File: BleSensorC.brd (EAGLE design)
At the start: 29.5 x 37.5 mm, 14 parts, among them IC1 SI7020-A10-GM, U1 PIC18(L)F14K22-SOIC

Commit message: Fusion 3D support
Fusion 3D support
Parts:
- removed JP2: (no value), pinhead:1X02/90
- removed U$3: SMTU2450N-LF, Battery holders:SMD2450
- added B1: SMTU2450N-LF.TR, esao:SMTU2450N-LF
- added C6: 1nF, resistor:C0805
- added C7: 1uF, resistor:C0805
- added MK1: SPH0644HM4H-1-3D, esao:SOJ88P324X95-6
- added Q1: SI2333DDS-T1-GE3, esao:SOT95P237X112-3
- added R4: 4k7, resistor:R0805
- added T1: BPW85C-L90, esao:LED-3MM
- C5: value 1nF -> 100nF
- IC1: value SI7020-A10-GM -> SI7020-A20-GM; device si70xx-10:DFN6-3X3 -> esao:SON100P300X300X80-7N
- JP1: value (none) -> PINHD-1X8; device pinhead:1X06 -> esao:1X08-S
- R1, R2, R3: device resistor:M0805 -> resistor:R0805
- U1: value PIC18(L)F14K22-SOIC -> PIC16LF18446-I_SS; device Microchip PIC18F12K44_esao:SOIC-20 -> SamacSys_Parts:SOP65P780X200-20
- U2: value (none) -> RN4871-I; device Microchip RN4871:RN4871 -> esao:RN4871
- moved C5 13.7 mm to (19.5, 2.81), turned to 90 degrees
- moved C3 9.97 mm to (21.1, 17.4)
- moved R1 6.00 mm to (8.13, 20.3)
- moved U1 5.86 mm to (18.8, 24.3), turned to 180 degrees
- moved R2 5.01 mm to (8.13, 24.3)
- moved R3 4.51 mm to (8.13, 28.9)
- moved C1 3.83 mm to (10.1, 34.2)
- moved C2 3.69 mm to (10.1, 37.8)
- moved U2 3.58 mm to (20.0, 37.0)
- moved JP1 2.29 mm to (29.0, 17.3)
- moved C4 0.71 mm to (14.1, 6.93), turned to 180 degrees
- moved IC1 0.44 mm to (14.4, 2.44), flipped to the top
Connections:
- net RA3_MCLR_VPP renamed !MCLR!_VPP_RA3
- removed net SCL: IC1.6, R3.2, U1.11
- removed net SDA: IC1.1, R2.2, U1.13
- removed net U_MON: U1.17
- new net +B: B1.+B, Q1.3
- new net SCL1: IC1.6, R3.2, U1.16
- new net SCL2: MK1.2, U1.8
- new net SDA1: IC1.1, R2.2, U1.15
- new net SDA2: MK1.3, U1.9
- net GND: now also B1.-B, C6.2, C7.2, IC1.7, MK1.4, MK1.6, Q1.1; no longer U$3.B-
- net IMP: now also C6.1, T1.K; no longer C5.1, JP2.2
- net PIC_RX: now also U1.5; no longer U1.12
- net PIC_TX: now also U1.6; no longer U1.10
- net RST: now also C7.1, R4.1
- net UART_RX_IND: now also U1.7; no longer U1.16
- net VDD: now also C5.1, MK1.1, MK1.5, Q1.2, R4.2, T1.A; no longer JP2.1, U$3.B+
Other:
- board size 29.5 x 37.5 mm -> 29 x 40.5 mm

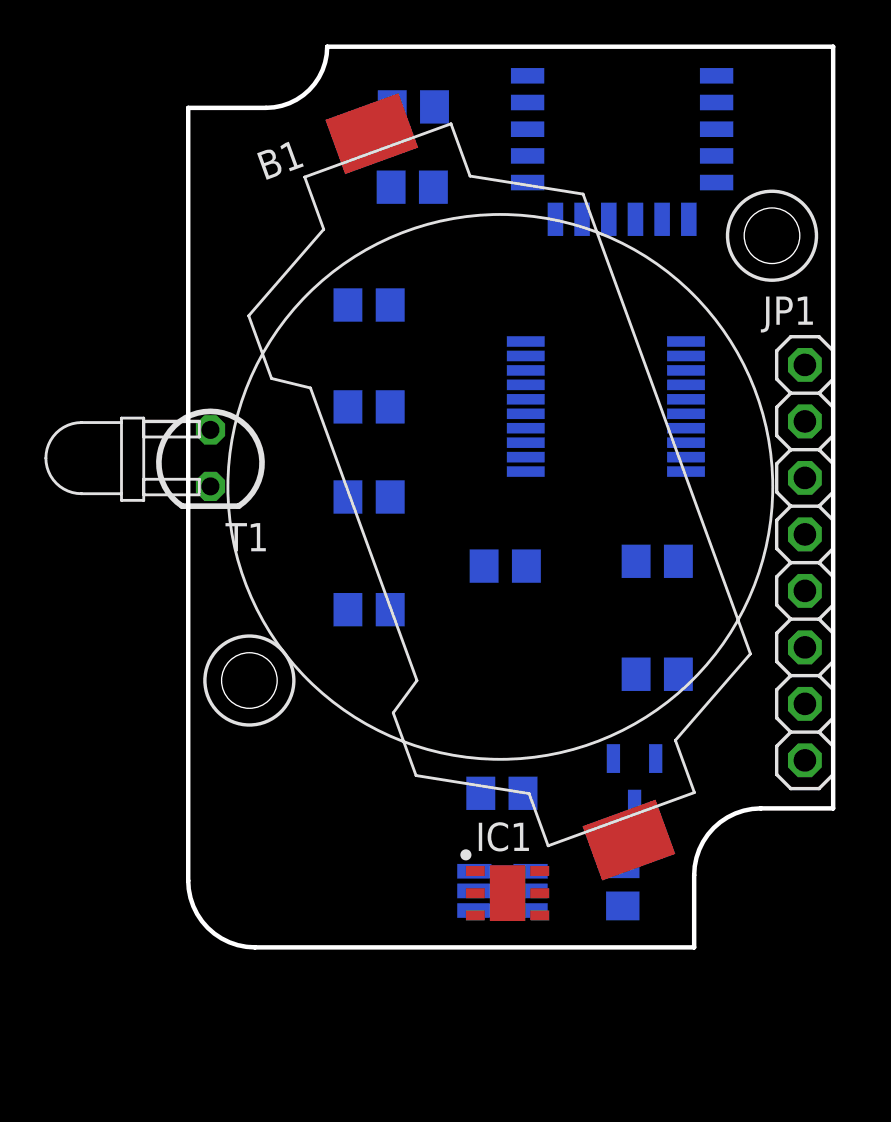
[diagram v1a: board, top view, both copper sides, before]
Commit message: JP1 & JP2
JP1 1X6
JP2 2X3
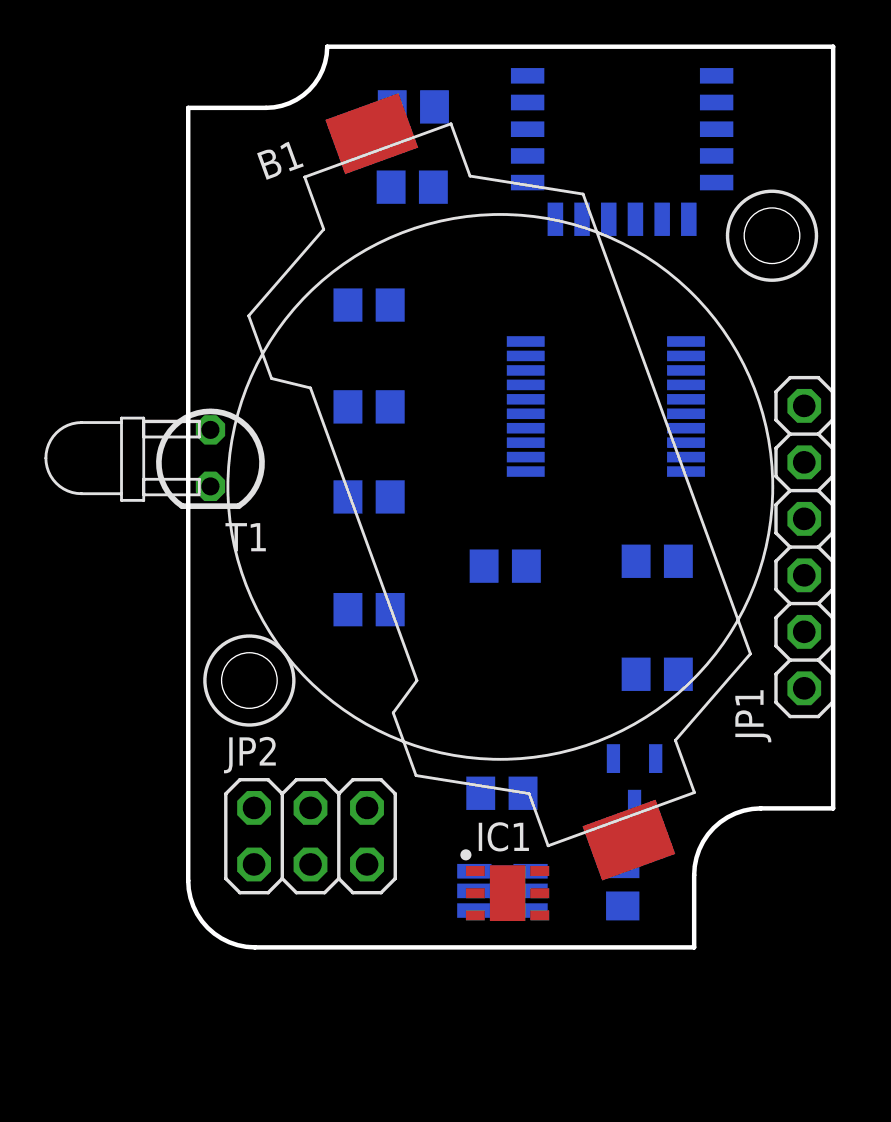
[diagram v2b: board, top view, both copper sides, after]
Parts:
- added JP2: (no value), pinhead:2X03
- JP1: value PINHD-1X8 -> (none); device esao:1X08-S -> esao:1X06-S
- moved JP1 1.48 mm to (27.7, 18.0), turned to 90 degrees
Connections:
- new net RB4: JP2.3
- new net RB5: JP2.4, U1.12
- new net RB6: JP2.5, U1.11
- new net RB7: JP2.6, U1.10
- net GND: now also JP2.2
- net VDD: now also JP2.1
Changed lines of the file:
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@@
 </layers>
 <board>
-<fusionsync huburn="a.cGVyc29uYWw6dWUyZDI5MmVj" projecturn="a.cGVyc29uYWw6dWUyZDI5MmVjIzIwMTgxMTA3MTU4OTE4ODMx" f3durn="urn:adsk.wipprod:dm.lineage:j9s_aim0THuc_P2TtWFECQ" pcbguid="5ee154ac-0536-47ce-9c18-78be7359e897" lastpulledtime="" lastsyncedchangeguid="e586453f-76b5-63cc-abac-863894cb1b87"/>
+<fusionsync huburn="a.cGVyc29uYWw6dWUyZDI5MmVj" projecturn="a.cGVyc29uYWw6dWUyZDI5MmVjIzIwMTgxMTA3MTU4OTE4ODMx" f3durn="urn:adsk.wipprod:dm.lineage:j9s_aim0THuc_P2TtWFECQ" pcbguid="5ee154ac-0536-47ce-9c18-78be7359e897" lastpulledtime="" lastsyncedchangeguid="8c282d48-1eb0-855c-9424-ff36f34d36e9"/>
 <plain>
 <circle x="2.75" y="12" radius="2" width="0.1524" layer="21"/>
@@
 </autorouter>
 <elements>
-<element name="JP1" library="esao" library_urn="urn:adsk.eagle:library:6645685" package="1X08-S" package3d_urn="urn:adsk.eagle:package:6645704/3" value="PINHD-1X8" x="29" y="17.3" smashed="yes" rot="R270">
-<attribute name="NAME" x="25.8288" y="27.9962" size="1.27" layer="25" ratio="10"/>
-<attribute name="VALUE" x="25.825" y="24.92" size="1.27" layer="27" rot="R270"/>
-</element>
 <element name="C1" library="resistor" library_urn="urn:adsk.eagle:library:348" package="C0805" package3d_urn="urn:adsk.eagle:package:23617/2" value="10uF" x="10.074" y="34.185" smashed="yes" rot="MR0">
 <attribute name="NAME" x="11.344" y="35.455" size="1.27" layer="26" rot="MR0"/>
@@
 <attribute name="VALUE" x="15.544253125" y="-0.985653125" size="1.27" layer="27" rot="R20"/>
 </element>
+<element name="JP1" library="esao" library_urn="urn:adsk.eagle:library:6645685" package="1X06-S" package3d_urn="urn:adsk.eagle:package:6884134/4" value="" x="27.7" y="18" smashed="yes" rot="R90">
+<attribute name="NAME" x="25.8712" y="9.3038" size="1.27" layer="25" ratio="10" rot="R90"/>
+<attribute name="VALUE" x="30.875" y="10.38" size="1.27" layer="27" rot="R90"/>
+</element>
+<element name="JP2" library="pinhead" library_urn="urn:adsk.eagle:library:325" package="2X03" package3d_urn="urn:adsk.eagle:package:22462/2" value="" x="5.5" y="5" smashed="yes">
+<attribute name="NAME" x="1.69" y="8.175" size="1.27" layer="25" ratio="10"/>
+<attribute name="VALUE" x="1.69" y="0.555" size="1.27" layer="27"/>
+</element>
 </elements>
 <signals>
 <signal name="VDD">
-<contactref element="JP1" pad="2"/>
 <contactref element="MK1" pad="1"/>
 <contactref element="IC1" pad="5"/>
@@
 <contactref element="U2" pad="14"/>
 <contactref element="T1" pad="A"/>
-<wire x1="22.04" y1="17.361" x2="27.73" y2="23.65" width="0" layer="19" extent="16-16"/>
-<wire x1="15.1771" y1="21.395" x2="22.04" y2="17.361" width="0" layer="19" extent="16-16"/>
+<contactref element="JP1" pad="2"/>
+<contactref element="JP2" pad="1"/>
+<wire x1="11.074" y1="37.793" x2="15.26" y2="36.79" width="0" layer="19" extent="16-16"/>
+<wire x1="11.024" y1="34.185" x2="11.074" y2="37.793" width="0" layer="19" extent="16-16"/>
+<wire x1="15.1771" y1="21.395" x2="11.024" y2="34.185" width="0" layer="19" extent="16-16"/>
+<wire x1="22.04" y1="17.361" x2="15.1771" y2="21.395" width="0" layer="19" extent="16-16"/>
 <wire x1="20.14" y1="12.281" x2="22.04" y2="17.361" width="0" layer="19" extent="16-16"/>
 <wire x1="21.02" y1="8.4916" x2="20.14" y2="12.281" width="0" layer="19" extent="16-16"/>
+<wire x1="27.7" y1="14.19" x2="22.04" y2="17.361" width="0" layer="19" extent="16-16"/>
 <wire x1="19.54" y1="1.865" x2="21.02" y2="8.4916" width="0" layer="19" extent="16-16"/>
 <wire x1="15.811" y1="2.436" x2="19.54" y2="1.865" width="0" layer="19" extent="1-16"/>
@@
 <wire x1="12.8664" y1="1.656" x2="15.3936" y2="2.54" width="0" layer="19" extent="16-16"/>
 <wire x1="13.155" y1="6.929" x2="15.3936" y2="2.54" width="0" layer="19" extent="16-16"/>
+<wire x1="2.96" y1="3.73" x2="12.8664" y2="1.656" width="0" layer="19" extent="16-16"/>
 <wire x1="1" y1="23.27" x2="15.1771" y2="21.395" width="0" layer="19" extent="16-16"/>
-<wire x1="11.024" y1="34.185" x2="15.1771" y2="21.395" width="0" layer="19" extent="16-16"/>
-<wire x1="11.074" y1="37.793" x2="11.024" y2="34.185" width="0" layer="19" extent="16-16"/>
-<wire x1="15.26" y1="36.79" x2="11.074" y2="37.793" width="0" layer="19" extent="16-16"/>
 </signal>
 <signal name="!MCLR!_VPP_RA3">
+<contactref element="U1" pad="4"/>
 <contactref element="JP1" pad="1"/>
-<contactref element="U1" pad="4"/>
-<wire x1="15.1771" y1="23.345" x2="27.73" y2="26.19" width="0" layer="19" extent="16-16"/>
+<wire x1="27.7" y1="11.65" x2="15.1771" y2="23.345" width="0" layer="19" extent="16-16"/>
 </signal>
 <signal name="GND">
-<contactref element="JP1" pad="3"/>
 <contactref element="IC1" pad="2"/>
 <contactref element="C6" pad="2"/>
@@
 <contactref element="IC1" pad="7"/>
 <contactref element="B1" pad="-B"/>
+<contactref element="JP1" pad="3"/>
+<contactref element="JP2" pad="2"/>
 <wire x1="15.26" y1="35.59" x2="23.76" y2="37.99" width="0" layer="19" extent="16-16"/>
-<wire x1="9.174" y1="37.793" x2="15.26" y2="35.59" width="0" layer="19" extent="16-16"/>
-<wire x1="9.124" y1="34.185" x2="9.174" y2="37.793" width="0" layer="19" extent="16-16"/>
+<wire x1="9.124" y1="34.185" x2="15.26" y2="35.59" width="0" layer="19" extent="16-16"/>
+<wire x1="9.174" y1="37.793" x2="9.124" y2="34.185" width="0" layer="19" extent="16-16"/>
 <wire x1="9.082" y1="28.884" x2="9.124" y2="34.185" width="0" layer="19" extent="16-16"/>
 <wire x1="9.082" y1="24.304" x2="9.082" y2="28.884" width="0" layer="19" extent="16-16"/>
 <wire x1="9.082" y1="20.254" x2="9.082" y2="24.304" width="0" layer="19" extent="16-16"/>
+<wire x1="13.305" y1="17.144" x2="9.082" y2="20.254" width="0" layer="19" extent="16-16"/>
 <wire x1="7.182" y1="15.186" x2="9.082" y2="20.254" width="0" layer="19" extent="16-16"/>
-<wire x1="13.305" y1="17.144" x2="7.182" y2="15.186" width="0" layer="19" extent="16-16"/>
-<wire x1="15.055" y1="6.929" x2="13.305" y2="17.144" width="0" layer="19" extent="16-16"/>
-<wire x1="19.12" y1="8.4916" x2="15.055" y2="6.929" width="0" layer="19" extent="16-16"/>
-<wire x1="15.3936" y1="3.424" x2="15.055" y2="6.929" width="0" layer="19" extent="16-16"/>
-<wire x1="14.361" y1="2.436" x2="15.3936" y2="3.424" width="0" layer="19" extent="1-16"/>
-<wire x1="12.911" y1="2.436" x2="14.361" y2="2.436" width="0" layer="19" extent="1-1"/>
-<wire x1="15.3936" y1="1.656" x2="14.361" y2="2.436" width="0" layer="19" extent="1-16"/>
-<wire x1="19.54" y1="3.765" x2="15.3936" y2="3.424" width="0" layer="19" extent="16-16"/>
 <wire x1="20.14" y1="17.361" x2="13.305" y2="17.144" width="0" layer="19" extent="16-16"/>
 <wire x1="22.3829" y1="21.395" x2="20.14" y2="17.361" width="0" layer="19" extent="16-16"/>
-<wire x1="27.73" y1="21.11" x2="22.3829" y2="21.395" width="0" layer="19" extent="16-16"/>
-<wire x1="19.814340625" y1="4.825225" x2="7.182" y2="15.186" width="0" layer="19" extent="1-16"/>
+<wire x1="27.7" y1="16.73" x2="22.3829" y2="21.395" width="0" layer="19" extent="16-16"/>
+<wire x1="19.12" y1="8.4916" x2="20.14" y2="17.361" width="0" layer="19" extent="16-16"/>
+<wire x1="19.814340625" y1="4.825225" x2="19.12" y2="8.4916" width="0" layer="19" extent="1-16"/>
+<wire x1="19.54" y1="3.765" x2="19.814340625" y2="4.825225" width="0" layer="19" extent="1-16"/>
+<wire x1="15.3936" y1="3.424" x2="19.54" y2="3.765" width="0" layer="19" extent="16-16"/>
+<wire x1="14.361" y1="2.436" x2="15.3936" y2="3.424" width="0" layer="19" extent="1-16"/>
+<wire x1="15.3936" y1="1.656" x2="14.361" y2="2.436" width="0" layer="19" extent="1-16"/>
+<wire x1="12.911" y1="2.436" x2="14.361" y2="2.436" width="0" layer="19" extent="1-1"/>
+<wire x1="15.055" y1="6.929" x2="15.3936" y2="3.424" width="0" layer="19" extent="16-16"/>
+<wire x1="2.96" y1="6.27" x2="7.182" y2="15.186" width="0" layer="19" extent="16-16"/>
 </signal>
 <signal name="RA1_ICSPCLK">
+<contactref element="U1" pad="18"/>
 <contactref element="JP1" pad="5"/>
-<contactref element="U1" pad="18"/>
-<wire x1="22.3829" y1="22.695" x2="27.73" y2="16.03" width="0" layer="19" extent="16-16"/>
+<wire x1="27.7" y1="21.81" x2="22.3829" y2="22.695" width="0" layer="19" extent="16-16"/>
 </signal>
 <signal name="RA4_TIG">
+<contactref element="U1" pad="3"/>
 <contactref element="JP1" pad="6"/>
-<contactref element="U1" pad="3"/>
-<wire x1="15.1771" y1="22.695" x2="27.73" y2="13.49" width="0" layer="19" extent="16-16"/>
+<wire x1="15.1771" y1="22.695" x2="27.7" y2="24.35" width="0" layer="19" extent="16-16"/>
 </signal>
 <signal name="RA0_ICSPDAT">
+<contactref element="U1" pad="19"/>
 <contactref element="JP1" pad="4"/>
-<contactref element="U1" pad="19"/>
-<wire x1="22.3829" y1="22.045" x2="27.73" y2="18.57" width="0" layer="19" extent="16-16"/>
+<wire x1="27.7" y1="19.27" x2="22.3829" y2="22.045" width="0" layer="19" extent="16-16"/>
 </signal>
 <signal name="PIC_RX">
@@
 <wire x1="8.254059375" y1="36.586834375" x2="20.07" y2="6.4384" width="0" layer="19" extent="1-16"/>
 </signal>
+<signal name="RB5">
+<contactref element="U1" pad="12"/>
+<contactref element="JP2" pad="4"/>
+<wire x1="5.5" y1="6.27" x2="22.3829" y2="26.595" width="0" layer="19" extent="16-16"/>
+</signal>
+<signal name="RB6">
+<contactref element="U1" pad="11"/>
+<contactref element="JP2" pad="5"/>
+<wire x1="8.04" y1="3.73" x2="22.3829" y2="27.245" width="0" layer="19" extent="16-16"/>
+</signal>
+<signal name="RB7">
+<contactref element="U1" pad="10"/>
+<contactref element="JP2" pad="6"/>
+<wire x1="8.04" y1="6.27" x2="15.1771" y2="27.245" width="0" layer="19" extent="16-16"/>
+</signal>
+<signal name="RB4">
+<contactref element="JP2" pad="3"/>
+</signal>
 </signals>

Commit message: T1 phototransistor
Changed T1 to Vishay VEMT2523
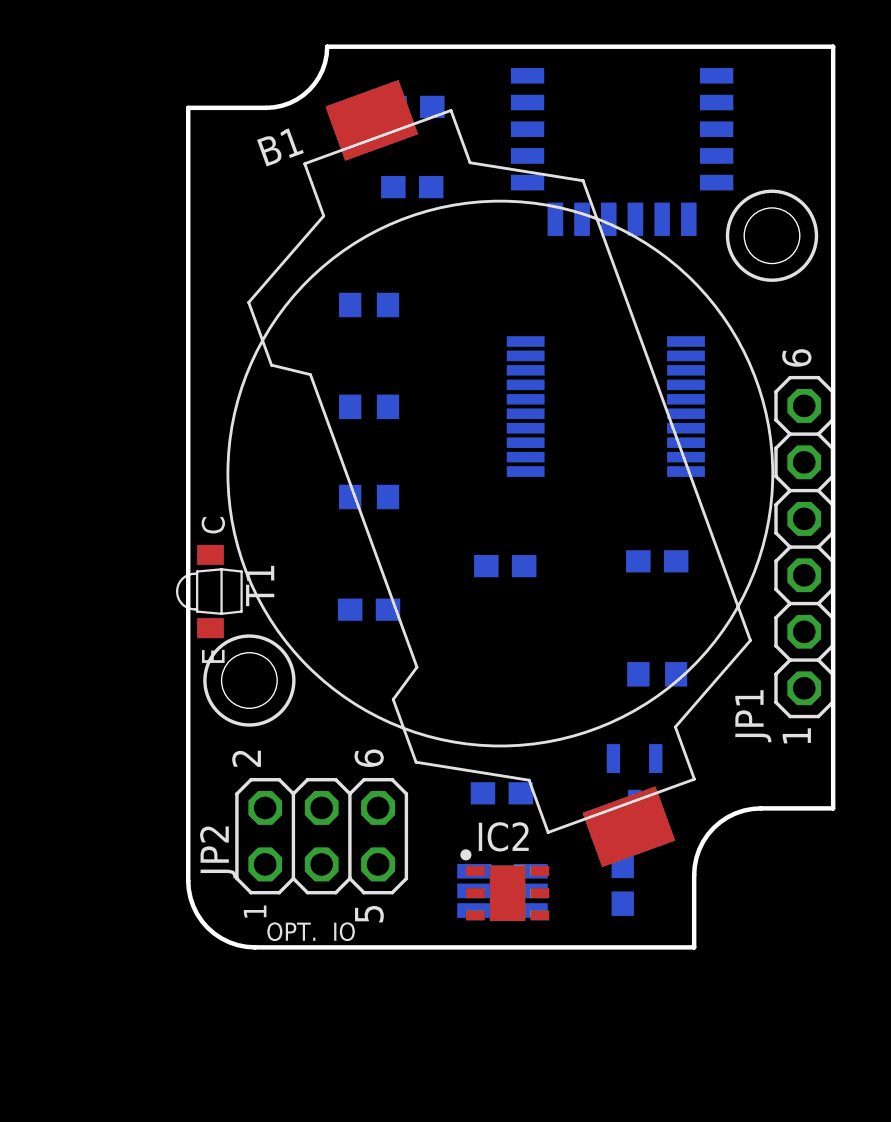
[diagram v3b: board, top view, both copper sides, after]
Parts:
- removed U2: RN4871-I, esao:RN4871
- added IC2: SI7020-A20-GM, esao:DFN-6-3X3-SI7020
- C1: value 10uF -> 1nF; device resistor:C0805 -> resistor:C0603
- C2: value 100nF -> 10uF; device resistor:C0805 -> resistor:C0603
- C3, C4, C5, C7: device resistor:C0805 -> resistor:C0603
- C6: value 1nF -> 100nF; device resistor:C0805 -> resistor:C0603
- IC1: value SI7020-A20-GM -> PIC16LF18446-I_SS; device esao:SON100P300X300X80-7N -> SamacSys_Parts:SOP65P780X200-20
- R1, R2, R3, R4: device resistor:R0805 -> resistor:R0603
- T1: value BPW85C-L90 -> VEMT2523SLX01; device esao:LED-3MM -> esao:VEMT2523SL
- U1: value PIC16LF18446-I_SS -> RN4871-I; device SamacSys_Parts:SOP65P780X200-20 -> esao:RN4871
- moved C3 23.2 mm to (10.1, 37.8)
- moved IC1 22.3 mm to (18.8, 24.3), flipped to the bottom, turned to 180 degrees
- moved C1 19.1 mm to (8.13, 15.2)
- moved C6 16.8 mm to (19.5, 2.81), turned to 90 degrees
- moved U1 12.7 mm to (20.0, 37.0), turned to 0 degrees
- moved C4 12.6 mm to (21.1, 17.4), turned to 0 degrees
- moved C5 6.82 mm to (14.1, 6.93), turned to 180 degrees
- moved T1 6.00 mm to (1.00, 16.0), turned to 270 degrees
- moved C2 3.61 mm to (10.1, 34.2)
- moved B1 0.60 mm to (14.0, 21.4)
- moved JP2 0.50 mm to (6.00, 5.00)
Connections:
- net !MCLR!_VPP_RA3: now also IC1.4; no longer U1.4
- net GND: now also IC1.20, IC2.2, IC2.7, U1.13, U1.2; no longer IC1.2, IC1.7, U1.20, U2.13, U2.2
- net IMP: now also C1.1, IC1.2, JP2.3, T1.E; no longer C6.1, T1.K, U1.2
- net PIC_RX: now also IC1.5, U1.8; no longer U1.5, U2.8
- net PIC_TX: now also IC1.6, U1.7; no longer U1.6, U2.7
- net RA0_ICSPDAT: now also IC1.19; no longer U1.19
- net RA1_ICSPCLK: now also IC1.18; no longer U1.18
- net RA4_TIG: now also IC1.3; no longer U1.3
- net RB4: now also JP2.4; no longer JP2.3
- net RB5: now also IC1.12, JP2.5; no longer JP2.4, U1.12
- net RB6: now also IC1.11, JP2.6; no longer JP2.5, U1.11
- net RB7: now also IC1.10; no longer JP2.6, U1.10
- net RST: now also U1.10; no longer U2.10
- net SCL1: now also IC1.16, IC2.6; no longer IC1.6, U1.16
- net SCL2: now also IC1.8; no longer U1.8
- net SDA1: now also IC1.15, IC2.1; no longer IC1.1, U1.15
- net SDA2: now also IC1.9; no longer U1.9
- net UART_RX_IND: now also IC1.7, U1.6; no longer U1.7, U2.6
- net VDD: now also C6.1, IC1.1, IC2.5, T1.C, U1.14; no longer C1.1, IC1.5, T1.A, U1.1, U2.14
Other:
- board text added: "1"
- board text added: "2"
- board text added: "5"
- board text added: "6"
- board text added: "OPT. IO"

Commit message: Manual routing
Manual routing
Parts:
- moved Q1 29.8 mm to (4.75, 33.0), turned to 0 degrees
- moved R3 19.3 mm to (22.0, 15.5)
- moved R2 18.9 mm to (22.0, 11.5)
- moved R4 16.5 mm to (9.00, 23.5)
- moved C7 11.6 mm to (9.00, 27.5)
- moved C4 6.62 mm to (14.5, 18.0)
- moved R1 2.42 mm to (9.00, 18.0)
- moved C2 2.19 mm to (10.0, 32.0), turned to 180 degrees
- moved C3 1.80 mm to (10.0, 36.0), turned to 180 degrees
- moved C1 1.47 mm to (9.00, 14.0), turned to 180 degrees
- moved JP2 1.00 mm to (6.00, 4.00)
- moved U1 0.50 mm to (20.0, 37.5)
- moved C5 0.40 mm to (14.5, 7.00)
- moved IC1 0.39 mm to (19.0, 24.0)
- moved C6 0.19 mm to (19.5, 3.00)
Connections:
- net RB4: now also IC1.13
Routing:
- net VDD: track 0.00 -> 123.0 mm, vias 0 -> 2
- net IMP: track 0.00 -> 42.1 mm, vias 0 -> 1
- net SDA1: track 0.00 -> 30.9 mm, vias 0 -> 1
- net RB5: track 0.00 -> 30.1 mm, vias 0 -> 1
- net RB6: track 0.00 -> 29.7 mm, vias 0 -> 1
- net !MCLR!_VPP_RA3: track 0.00 -> 29.6 mm, vias 0 -> 1
- net RB4: track 0.00 -> 28.8 mm, vias 0 -> 1
- net SCL2: track 0.00 -> 27.7 mm, vias 0 -> 3
- net SDA2: track 0.00 -> 26.7 mm, vias 0 -> 2
- net SCL1: track 0.00 -> 25.3 mm, vias 0 -> 1
- net PIC_RX: track 0.00 -> 19.8 mm
- net PIC_TX: track 0.00 -> 19.3 mm
- net RA4_TIG: track 0.00 -> 17.3 mm
- net RST: track 0.00 -> 15.8 mm
- net UART_RX_IND: track 0.00 -> 12.0 mm
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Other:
- outline, holes or cut-outs redrawn
- board text added: "BLE SENSOR C v1.00"
